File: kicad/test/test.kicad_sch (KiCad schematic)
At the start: 48 parts, among them J1 RJ45, J10 Conn_02x06_Odd_Even, J2 RJ45, J3 Conn_02x06_Odd_Even, J4 Conn_02x06_Odd_Even, J5 Conn_02x06_Odd_Even, J6 Conn_02x06_Odd_Even, J7 Conn_02x06_Odd_Even, J8 Conn_02x06_Odd_Even, J9 Conn_02x06_Odd_Even, U1 SN65LVDS049, U3 TLC5971PWP, U4 MIC5504-3.3YM5

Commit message: V1.0
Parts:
- added J11: Conn_01x02_Pin, Connector_PinSocket_2.54mm:PinSocket_1x02_P2.54mm_Vertical, symbol Connector:Conn_01x02_Pin
- added R17: 0, Resistor_SMD:R_0805_2012Metric, symbol Device:R
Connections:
- net +5V: now also J11.1 (Pin_1), R17.2; no longer R10.1, R11.1, R12.1, R13.1, R14.1, R15.1, R16.1, R5.1, R6.1, R7.1, R8.1, R9.1
- new net: J11.2 (Pin_2), R10.1, R11.1, R12.1, R13.1, R14.1, R15.1, R16.1, R17.1, R5.1, R6.1, R7.1, R8.1, R9.1
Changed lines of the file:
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@@
 	)
 	(junction
+		(at 144.78 96.52)
+		(diameter 0)
+		(color 0 0 0 0)
+	)
+	(junction
 		(at 60.96 62.23)
 		(diameter 0)
@@
 	(wire
 		(pts
+			(xy 144.78 93.98) (xy 144.78 96.52)
+		)
+		(stroke
+			(width 0)
+			(type default)
+		)
+	)
+	(wire
+		(pts
 			(xy 55.88 69.85) (xy 63.5 69.85)
 		)
@@
 	(wire
 		(pts
+			(xy 156.21 96.52) (xy 160.02 96.52)
+		)
+		(stroke
+			(width 0)
+			(type default)
+		)
+	)
+	(wire
+		(pts
 			(xy 236.22 118.11) (xy 228.6 118.11)
 		)
@@
 	(wire
 		(pts
+			(xy 160.02 96.52) (xy 160.02 101.6)
+		)
+		(stroke
+			(width 0)
+			(type default)
+		)
+	)
+	(wire
+		(pts
 			(xy 62.23 119.38) (xy 62.23 121.92)
 		)
@@
 	(wire
 		(pts
+			(xy 144.78 99.06) (xy 144.78 101.6)
+		)
+		(stroke
+			(width 0)
+			(type default)
+		)
+	)
+	(wire
+		(pts
 			(xy 215.9 120.65) (xy 195.58 120.65)
 		)
@@
 	(wire
 		(pts
+			(xy 139.7 99.06) (xy 144.78 99.06)
+		)
+		(stroke
+			(width 0)
+			(type default)
+		)
+	)
+	(wire
+		(pts
 			(xy 139.7 101.6) (xy 139.7 102.87)
 		)
@@
 	(wire
 		(pts
+			(xy 144.78 96.52) (xy 148.59 96.52)
+		)
+		(stroke
+			(width 0)
+			(type default)
+		)
+	)
+	(wire
+		(pts
 			(xy 96.52 64.77) (xy 95.25 64.77)
 		)
@@
 	(wire
 		(pts
+			(xy 139.7 96.52) (xy 144.78 96.52)
+		)
+		(stroke
+			(width 0)
+			(type default)
+		)
+	)
+	(wire
+		(pts
 			(xy 236.22 60.96) (xy 228.6 60.96)
 		)
@@
 	(wire
 		(pts
-			(xy 160.02 99.06) (xy 160.02 101.6)
-		)
-		(stroke
-			(width 0)
-			(type default)
-		)
-	)
-	(wire
-		(pts
 			(xy 149.86 120.65) (xy 149.86 142.24)
 		)
@@
 	(symbol
 		(lib_id "power:+5V")
-		(at 160.02 99.06 0)
+		(at 144.78 93.98 0)
 		(unit 1)
 		(exclude_from_sim no)
@@
 		(fields_autoplaced yes)
 		(property "Reference" "#PWR04"
-			(at 160.02 102.87 0)
+			(at 144.78 97.79 0)
 			(effects
 				(font
@@
 		)
 		(property "Value" "+5V"
-			(at 160.02 93.98 0)
+			(at 144.78 88.9 0)
 			(effects
 				(font
@@
 		)
 		(property "Footprint" ""
-			(at 160.02 99.06 0)
+			(at 144.78 93.98 0)
 			(effects
 				(font
@@
 		)
 		(property "Datasheet" ""
-			(at 160.02 99.06 0)
+			(at 144.78 93.98 0)
 			(effects
 				(font
@@
 		)
 		(property "Description" ""
-			(at 160.02 99.06 0)
+			(at 144.78 93.98 0)
 			(effects
 				(font
@@
 	)
 	(symbol
+		(lib_id "Connector:Conn_01x02_Pin")
+		(at 134.62 96.52 0)
+		(unit 1)
+		(exclude_from_sim no)
+		(in_bom yes)
+		(on_board yes)
+		(dnp no)
+		(property "Reference" "J11"
+			(at 136.652 93.218 0)
+			(effects
+				(font
+					(size 1.27 1.27)
+				)
+			)
+		)
+		(property "Value" "Conn_01x02_Pin"
+			(at 135.255 93.98 0)
+			(effects
+				(font
+					(size 1.27 1.27)
+				)
+				(hide yes)
+			)
+		)
+		(property "Footprint" "Connector_PinSocket_2.54mm:PinSocket_1x02_P2.54mm_Vertical"
+			(at 134.62 96.52 0)
+			(effects
+				(font
+					(size 1.27 1.27)
+				)
+				(hide yes)
+			)
+		)
+		(property "Datasheet" "~"
+			(at 134.62 96.52 0)
+			(effects
+				(font
+					(size 1.27 1.27)
+				)
+				(hide yes)
+			)
+		)
+		(property "Description" "Generic connector, single row, 01x02, script generated"
+			(at 134.62 96.52 0)
+			(effects
+				(font
+					(size 1.27 1.27)
+				)
+				(hide yes)
+			)
+		)
+		(pin "2"
+		)
+		(pin "1"
+		)
+		(instances
+			(project "test"
+				(path "/bfb88c66-3278-41a9-b822-09be2f151e4c"
+					(reference "J11")
+					(unit 1)
+				)
+			)
+		)
+	)
+	(symbol
 		(lib_id "Connector:RJ45")
 		(at 45.72 59.69 0)
@@
 					(unit 1)
 				)
+			)
+		)
+	)
+	(symbol
+		(lib_id "Device:R")
+		(at 152.4 96.52 270)
+		(unit 1)
+		(exclude_from_sim no)
+		(in_bom yes)
+		(on_board yes)
+		(dnp no)
+		(property "Reference" "R17"
+			(at 152.4 93.98 90)
+			(effects
+				(font
+					(size 1.27 1.27)
+				)
+			)
+		)
+		(property "Value" "0"
+			(at 152.4 96.52 90)
+			(effects
+				(font
+					(size 1.27 1.27)
+				)
+			)
+		)
+		(property "Footprint" "Resistor_SMD:R_0805_2012Metric"
+			(at 152.4 94.742 90)
+			(effects
+				(font
+					(size 1.27 1.27)
+				)
+				(hide yes)
+			)
+		)
+		(property "Datasheet" "~"
+			(at 152.4 96.52 0)
+			(effects
+				(font
+					(size 1.27 1.27)
+				)
+				(hide yes)
+			)
+		)
+		(property "Description" ""
+			(at 152.4 96.52 0)
+			(effects
+				(font
+					(size 1.27 1.27)
+				)
+				(hide yes)
+			)
+		)
+		(pin "1"
+		)
+		(pin "2"
+		)
+		(instances
+			(project "test"
+				(path "/bfb88c66-3278-41a9-b822-09be2f151e4c"
+					(reference "R17")
+					(unit 1)
+				)

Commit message: Cleanup
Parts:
- removed R10, R11, R12, R13, R14, R15, R16, R5, R6, R7, R8, R9: 330, Resistor_SMD:R_0805_2012Metric, symbol Device:R
- removed U4: MIC5504-3.3YM5, Package_TO_SOT_SMD:SOT-23-5, symbol Regulator_Linear:MIC5504-3.3YM5
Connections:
- net +5V is gone; now on net +3V3: C1.1, C2.1, J1.5, J1.7, J10.10 (Pin_10), J10.12 (Pin_12), J10.2 (Pin_2), J10.4 (Pin_4), J10.6 (Pin_6), J10.8 (Pin_8), J11.1 (Pin_1), J2.5, J2.7, J3.10 (Pin_10), J3.12 (Pin_12), J3.2 (Pin_2), J3.4 (Pin_4), J3.6 (Pin_6), J3.8 (Pin_8), J4.10 (Pin_10), J4.12 (Pin_12), J4.2 (Pin_2), J4.4 (Pin_4), J4.6 (Pin_6), J4.8 (Pin_8), J5.10 (Pin_10), J5.12 (Pin_12), J5.2 (Pin_2), J5.4 (Pin_4), J5.6 (Pin_6), J5.8 (Pin_8), J6.10 (Pin_10), J6.12 (Pin_12), J6.2 (Pin_2), J6.4 (Pin_4), J6.6 (Pin_6), J6.8 (Pin_8), J7.10 (Pin_10), J7.12 (Pin_12), J7.2 (Pin_2), J7.4 (Pin_4), J7.6 (Pin_6), J7.8 (Pin_8), J8.10 (Pin_10), J8.12 (Pin_12), J8.2 (Pin_2), J8.4 (Pin_4), J8.6 (Pin_6), J8.8 (Pin_8), J9.10 (Pin_10), J9.12 (Pin_12), J9.2 (Pin_2), J9.4 (Pin_4), J9.6 (Pin_6), J9.8 (Pin_8), R17.2, U3.19 (VCC)
- net at J11.2 (Pin_2), R17.1: now also D10.2 (A), D11.2 (A), D12.2 (A), D13.2 (A), D2.2 (A), D3.2 (A), D4.2 (A), D5.2 (A), D6.2 (A), D7.2 (A), D8.2 (A), D9.2 (A)
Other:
- moved on the sheet: J11, R17

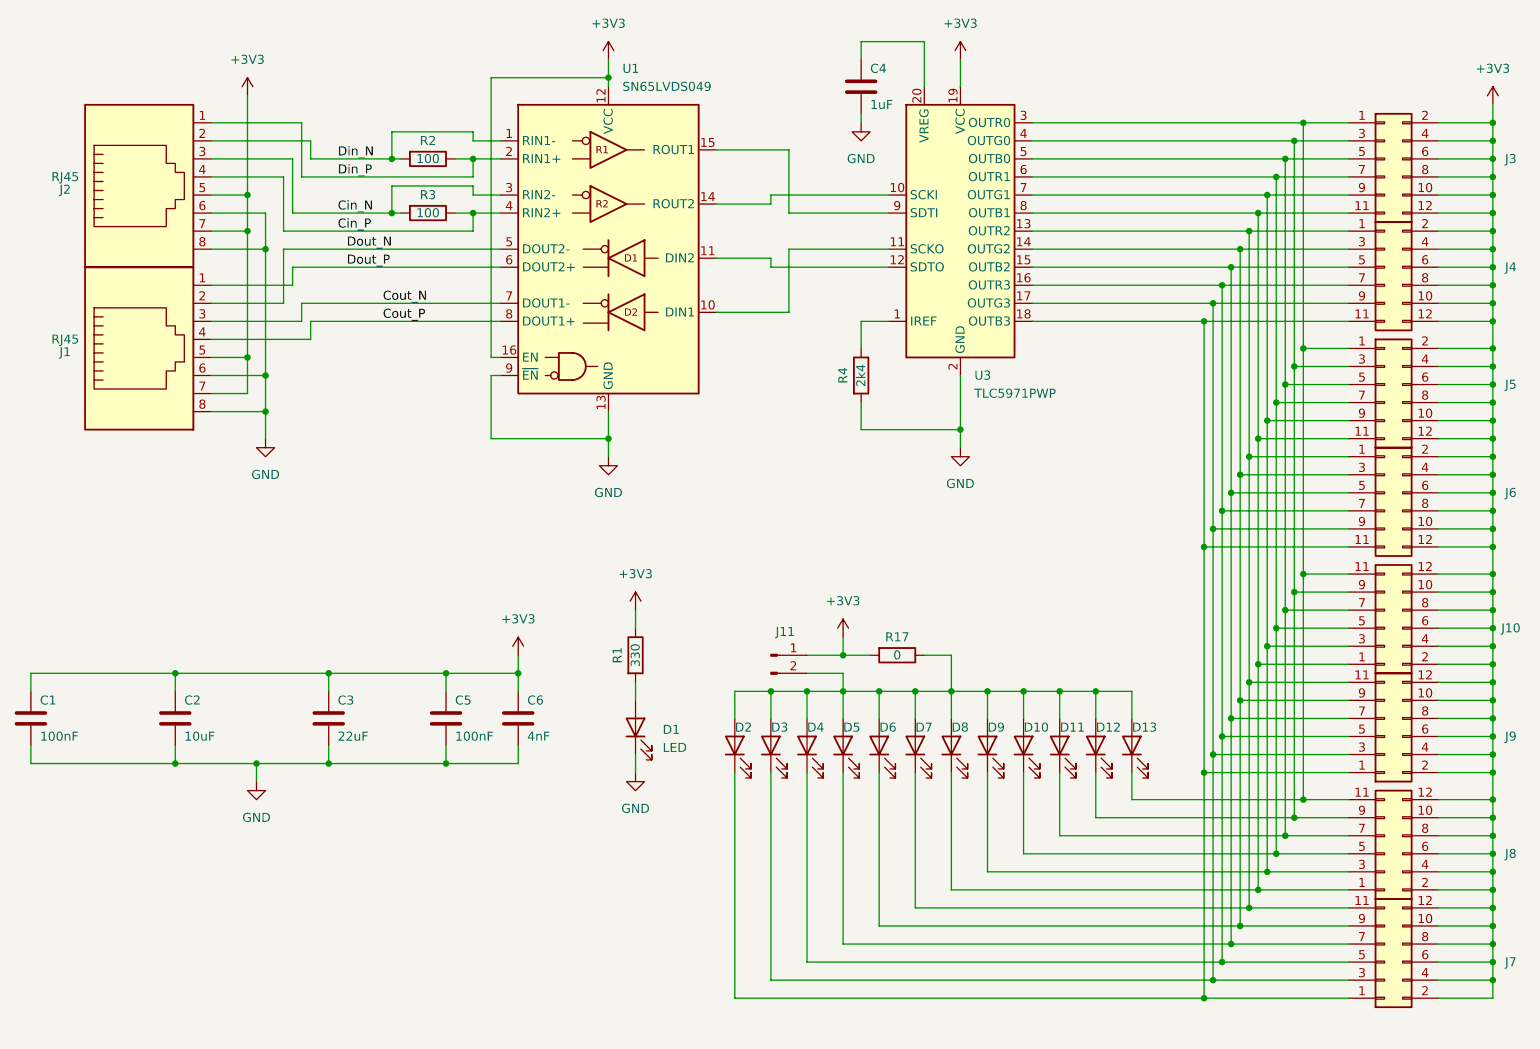
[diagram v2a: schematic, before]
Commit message: Fix led driver vcc
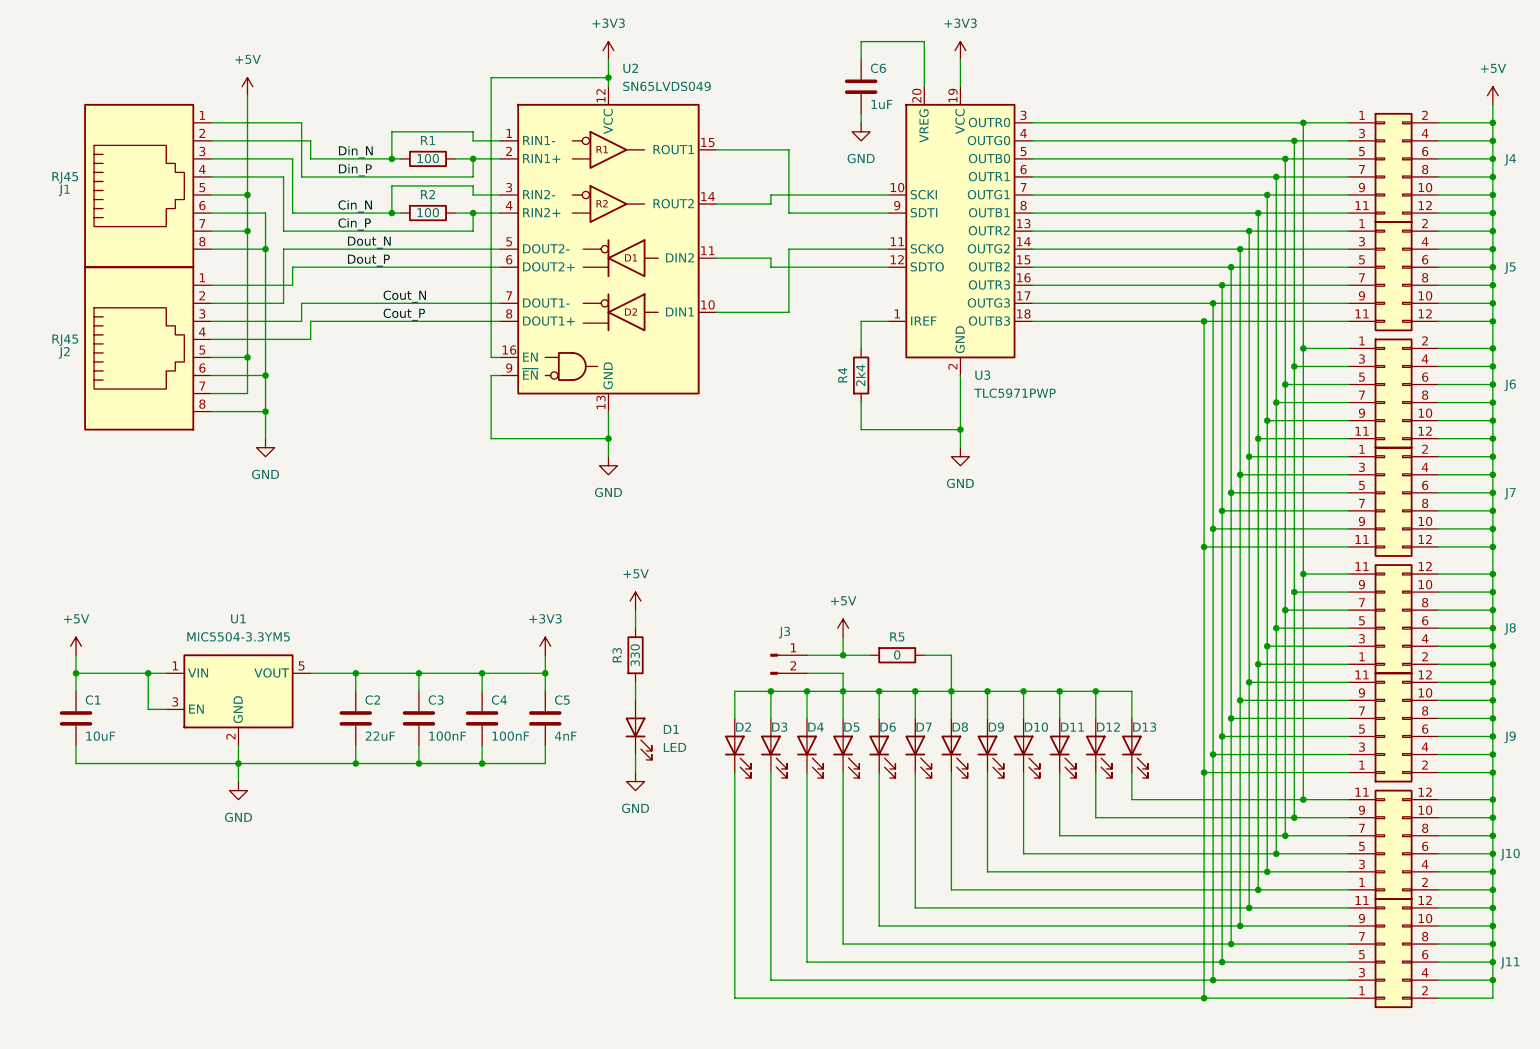
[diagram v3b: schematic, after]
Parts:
- added U1: MIC5504-3.3YM5, Package_TO_SOT_SMD:SOT-23-5, symbol Regulator_Linear:MIC5504-3.3YM5
- renumbered C2 to C1, C3 to C2, C1 to C3, C5 to C4, C6 to C5, C4 to C6, J2 to J1, J8 to J10, J7 to J11, J1 to J2, J11 to J3, J3 to J4, J4 to J5, J5 to J6, J6 to J7, J10 to J8, R2 to R1, R3 to R2, R1 to R3, R17 to R5, U1 to U2
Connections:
- net +3V3: now also U1.5 (VOUT); no longer C1.1, J1.5, J1.7, J10.10 (Pin_10), J10.12 (Pin_12), J10.2 (Pin_2), J10.4 (Pin_4), J10.6 (Pin_6), J10.8 (Pin_8), J11.10 (Pin_10), J11.12 (Pin_12), J11.2 (Pin_2), J11.4 (Pin_4), J11.6 (Pin_6), J11.8 (Pin_8), J2.5, J2.7, J3.1 (Pin_1), J4.10 (Pin_10), J4.12 (Pin_12), J4.2 (Pin_2), J4.4 (Pin_4), J4.6 (Pin_6), J4.8 (Pin_8), J5.10 (Pin_10), J5.12 (Pin_12), J5.2 (Pin_2), J5.4 (Pin_4), J5.6 (Pin_6), J5.8 (Pin_8), J6.10 (Pin_10), J6.12 (Pin_12), J6.2 (Pin_2), J6.4 (Pin_4), J6.6 (Pin_6), J6.8 (Pin_8), J7.10 (Pin_10), J7.12 (Pin_12), J7.2 (Pin_2), J7.4 (Pin_4), J7.6 (Pin_6), J7.8 (Pin_8), J8.10 (Pin_10), J8.12 (Pin_12), J8.2 (Pin_2), J8.4 (Pin_4), J8.6 (Pin_6), J8.8 (Pin_8), J9.10 (Pin_10), J9.12 (Pin_12), J9.2 (Pin_2), J9.4 (Pin_4), J9.6 (Pin_6), J9.8 (Pin_8), R3.1, R5.2
- net GND: now also U1.2 (GND)
- new net +5V: C1.1, J1.5, J1.7, J10.10 (Pin_10), J10.12 (Pin_12), J10.2 (Pin_2), J10.4 (Pin_4), J10.6 (Pin_6), J10.8 (Pin_8), J11.10 (Pin_10), J11.12 (Pin_12), J11.2 (Pin_2), J11.4 (Pin_4), J11.6 (Pin_6), J11.8 (Pin_8), J2.5, J2.7, J3.1 (Pin_1), J4.10 (Pin_10), J4.12 (Pin_12), J4.2 (Pin_2), J4.4 (Pin_4), J4.6 (Pin_6), J4.8 (Pin_8), J5.10 (Pin_10), J5.12 (Pin_12), J5.2 (Pin_2), J5.4 (Pin_4), J5.6 (Pin_6), J5.8 (Pin_8), J6.10 (Pin_10), J6.12 (Pin_12), J6.2 (Pin_2), J6.4 (Pin_4), J6.6 (Pin_6), J6.8 (Pin_8), J7.10 (Pin_10), J7.12 (Pin_12), J7.2 (Pin_2), J7.4 (Pin_4), J7.6 (Pin_6), J7.8 (Pin_8), J8.10 (Pin_10), J8.12 (Pin_12), J8.2 (Pin_2), J8.4 (Pin_4), J8.6 (Pin_6), J8.8 (Pin_8), J9.10 (Pin_10), J9.12 (Pin_12), J9.2 (Pin_2), J9.4 (Pin_4), J9.6 (Pin_6), J9.8 (Pin_8), R3.1, R5.2, U1.1 (VIN), U1.3 (EN)
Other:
- moved on the sheet: C1, C2, C3, C4, C5

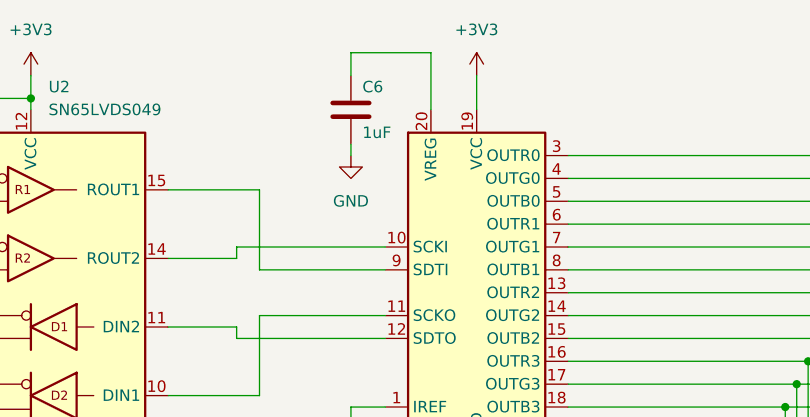
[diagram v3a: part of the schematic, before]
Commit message: fix vreg on led driver
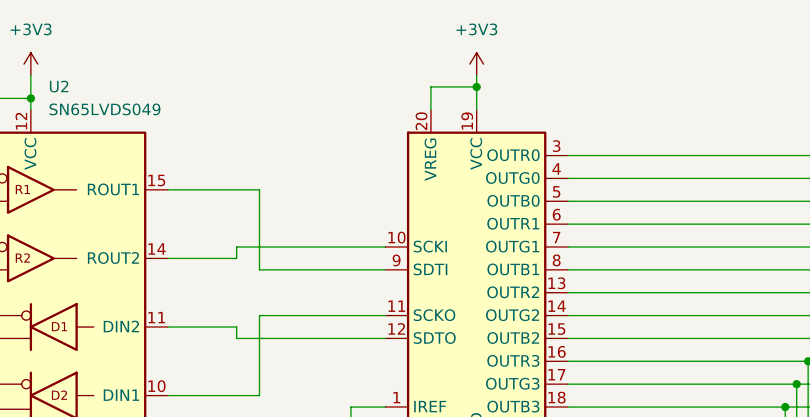
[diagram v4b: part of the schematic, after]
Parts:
- removed C6: 1uF, Capacitor_SMD:C_0805_2012Metric, symbol Device:C
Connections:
- net +3V3: now also U3.20 (VREG)
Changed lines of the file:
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@@
 	)
 	(junction
+		(at 161.29 21.59)
+		(diameter 0)
+		(color 0 0 0 0)
+	)
+	(junction
 		(at 204.47 39.37)
 		(diameter 0)
@@
 	(wire
 		(pts
-			(xy 161.29 20.32) (xy 161.29 24.13)
+			(xy 161.29 20.32) (xy 161.29 21.59)
 		)
 		(stroke
@@
 	(wire
 		(pts
+			(xy 156.21 21.59) (xy 161.29 21.59)
+		)
+		(stroke
+			(width 0)
+			(type default)
+		)
+	)
+	(wire
+		(pts
 			(xy 205.74 68.58) (xy 205.74 100.33)
 		)
@@
 	(wire
 		(pts
-			(xy 156.21 17.78) (xy 147.32 17.78)
-		)
-		(stroke
-			(width 0)
-			(type default)
-		)
-	)
-	(wire
-		(pts
 			(xy 236.22 71.12) (xy 236.22 68.58)
 		)
@@
 	(wire
 		(pts
-			(xy 147.32 27.94) (xy 147.32 29.21)
-		)
-		(stroke
-			(width 0)
-			(type default)
-		)
-	)
-	(wire
-		(pts
 			(xy 68.58 29.21) (xy 68.58 36.83)
 		)
@@
 	(wire
 		(pts
-			(xy 147.32 17.78) (xy 147.32 20.32)
-		)
-		(stroke
-			(width 0)
-			(type default)
-		)
-	)
-	(wire
-		(pts
 			(xy 200.66 78.74) (xy 200.66 110.49)
 		)
@@
 	(wire
 		(pts
+			(xy 161.29 21.59) (xy 161.29 24.13)
+		)
+		(stroke
+			(width 0)
+			(type default)
+		)
+	)
+	(wire
+		(pts
 			(xy 198.12 83.82) (xy 198.12 52.07)
 		)
@@
 	(wire
 		(pts
-			(xy 156.21 24.13) (xy 156.21 17.78)
+			(xy 156.21 24.13) (xy 156.21 21.59)
 		)
 		(stroke
@@
 	)
 	(symbol
-		(lib_id "power:GND")
-		(at 147.32 29.21 0)
-		(unit 1)
-		(exclude_from_sim no)
-		(in_bom yes)
-		(on_board yes)
-		(dnp no)
-		(fields_autoplaced yes)
-		(property "Reference" "#PWR011"
-			(at 147.32 35.56 0)
-			(effects
-				(font
-					(size 1.27 1.27)
-				)
-				(hide yes)
-			)
-		)
-		(property "Value" "GND"
-			(at 147.32 34.29 0)
-			(effects
-				(font
-					(size 1.27 1.27)
-				)
-			)
-		)
-		(property "Footprint" ""
-			(at 147.32 29.21 0)
-			(effects
-				(font
-					(size 1.27 1.27)
-				)
-				(hide yes)
-			)
-		)
-		(property "Datasheet" ""
-			(at 147.32 29.21 0)
-			(effects
-				(font
-					(size 1.27 1.27)
-				)
-				(hide yes)
-			)
-		)
-		(property "Description" ""
-			(at 147.32 29.21 0)
-			(effects
-				(font
-					(size 1.27 1.27)
-				)
-				(hide yes)
-			)
-		)
-		(pin "1"
-		)
-		(instances
-			(project "test"
-				(path "/bfb88c66-3278-41a9-b822-09be2f151e4c"
-					(reference "#PWR011")
-					(unit 1)
-				)
-			)
-		)
-	)
-	(symbol
 		(lib_id "power:+5V")
 		(at 36.83 104.14 0)
@@
 					(unit 1)
 				)
-			)
-		)
-	)
-	(symbol
-		(lib_id "Device:C")
-		(at 147.32 24.13 0)
-		(unit 1)
-		(exclude_from_sim no)
-		(in_bom yes)
-		(on_board yes)
-		(dnp no)
-		(property "Reference" "C6"
-			(at 148.59 21.59 0)
-			(effects
-				(font
-					(size 1.27 1.27)
-				)
-				(justify left)
-			)
-		)
-		(property "Value" "1uF"
-			(at 148.59 26.67 0)
-			(effects
-				(font
-					(size 1.27 1.27)
-				)
-				(justify left)
-			)
-		)
-		(property "Footprint" "Capacitor_SMD:C_0805_2012Metric"
-			(at 148.2852 27.94 0)
-			(effects
-				(font
-					(size 1.27 1.27)
-				)
-				(hide yes)
-			)
-		)
-		(property "Datasheet" "~"
-			(at 147.32 24.13 0)
-			(effects
-				(font
-					(size 1.27 1.27)
-				)
-				(hide yes)
-			)
-		)
-		(property "Description" ""
-			(at 147.32 24.13 0)
-			(effects
-				(font
-					(size 1.27 1.27)
-				)
-				(hide yes)
-			)
-		)
-		(pin "1"
-		)
-		(pin "2"
-		)
-		(instances
-			(project "test"
-				(path "/bfb88c66-3278-41a9-b822-09be2f151e4c"
-					(reference "C6")
-					(unit 1)
-				)
